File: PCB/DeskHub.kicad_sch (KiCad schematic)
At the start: 67 parts, among them J1 USB_A, J2 5V Barrel, U1 TUSB4041I, U2 3.3V Reg, U3 1.1V Reg, Y1 24MHz

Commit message: Completed schematic!
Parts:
- added R15, R20, R21, R22, R23, R24, R25, R26: 4.7K, symbol Device:R_Small
- added R27: 10K, symbol Device:R_Small
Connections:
- net BOARD_3.3V: now also R23.2, R24.2, R25.2, R26.2, R27.1
- net Earth: now also U1.65 (VSS), R15.2, R20.2, R21.2, R22.2
- net Port 1 Power Switch/PWRON_EN: now also R26.1
- net Port 2 Power Switch/PWRON_EN: now also R25.1
- net Port 3 Power Switch/PWRON_EN: now also R24.1
- net Port 4 Power Switch/PWRON_EN: now also R23.1
- net at U1.10 (GANGED/SMBA2/HS_UP): now also R21.1
- net at U1.13 (AUTOENz/HS_SUSPEND): now also R15.1
- net at U1.17 (TEST): now also R20.1
- net at U1.8 (FULLPWRMGMTz/SMBA1): now also R22.1
- net at U1.9 (PWRCTL_POL): now also R27.2
- no-connect marks 1 -> 4

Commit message: adjust schematic to match real components, assign footprints
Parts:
- removed Y1: 24MHz, symbol Device:Crystal
- added Y1: ECS-240-20-30B-TR, my_global:XTAL_ECS-240-20-30B-TR, symbol ECS-240-20-30B-TR:ECS-240-20-30B-TR
- C1, C16, C17, C43: footprint (none) -> Capacitor_SMD:C_0402_1005Metric
- C10, C11, C12, C18, C19, C2, C20, C21, C22, C23, C24, C25, C26, C28, C29, C3, C30, C31, C32, C33, C34, C35, C36, C37, C38, C39, C4, C40, C41, C5, C6, C7, C8, C9: footprint (none) -> Capacitor_SMD:C_0201_0603Metric
- C13, C14: value 18pF TODO -> 18pF; footprint (none) -> Capacitor_SMD:C_0402_1005Metric
- C15, C27, C42, C45, C46, C47: footprint (none) -> Capacitor_SMD:C_1206_3216Metric
- C44: footprint (none) -> Capacitor_SMD:C_0805_2012Metric
- D1, D2: footprint (none) -> LED_SMD:LED_0603_1608Metric
- FB5, FB6: footprint (none) -> my_global:BEADC1608X95N
- J1: footprint (none) -> my_global:61400416021; symbol Connector:USB_A -> 61400416021:61400416021
- J2: footprint (none) -> my_global:694108301002; symbol Connector:Barrel_Jack -> 694108301002:694108301002
- R1, R10, R15, R2, R20, R21, R22, R23, R24, R25, R26, R27, R3, R4, R5, R6, R7, R8, R9: footprint (none) -> Resistor_SMD:R_0402_1005Metric
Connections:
- net Earth: now also J2.3
- net GNDPWR: now also J1.S1, J1.S2; no longer J1.5 (Shield)
- net XI: now also Y1.3 (OUT/IN)
- net XO: now also Y1.1 (IN/OUT)
- no-connect marks 4 -> 6
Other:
- note added: "Crystal"
- note removed: "Crystal TODO calculate capacitor values"
- moved on the sheet: C13, C15

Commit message: final save of the night
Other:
- note added: "Design Notes - differential impedance of 90 Ohm - each differential pair should be 5*trace width apart - route all pairs on same layer, next to ground plane - avoid 90 degree bends, keep left and right bends equal - differential pairs should not exceed 50 mils relative distance"
- note removed: "Design Notes - differential impedance of 90Ohm - each differential pair should be 5*trace width apart - route all pairs on same layer, next to ground plane - avoid 90 degree bends, keep left and right bends equal - differential pairs should not exceed 50 mils relative distance"
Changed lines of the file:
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@@
 		)
 	)
-	(text "Design Notes\n\n- differential impedance of 90Ohm\n- each differential pair should be 5*trace width apart \n- route all pairs on same layer, next to ground plane\n- avoid 90 degree bends, keep left and right bends equal\n- differential pairs should not exceed 50 mils relative distance\n"
+	(text "Design Notes\n\n- differential impedance of 90 Ohm\n- each differential pair should be 5*trace width apart \n- route all pairs on same layer, next to ground plane\n- avoid 90 degree bends, keep left and right bends equal\n- differential pairs should not exceed 50 mils relative distance\n"
 		(exclude_from_sim no)
 		(at 124.46 -11.43 0)

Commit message: saved
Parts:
- C22: footprint Capacitor_SMD:C_0201_0603Metric -> Capacitor_SMD:C_1206_3216Metric
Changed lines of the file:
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@@
 		(polyline
 			(pts
-				(xy 171.45 138.43) (xy 171.45 143.51) (xy 172.72 143.51) (xy 172.72 138.43)
+				(xy 172.72 125.73) (xy 172.72 130.81) (xy 173.99 130.81) (xy 173.99 125.73)
 			)
 			(stroke
@@
 		(polyline
 			(pts
-				(xy 171.45 151.13) (xy 171.45 156.21) (xy 172.72 156.21) (xy 172.72 151.13)
+				(xy 171.45 163.83) (xy 171.45 168.91) (xy 172.72 168.91) (xy 172.72 163.83)
 			)
 			(stroke
@@
 		(polyline
 			(pts
-				(xy 172.72 125.73) (xy 172.72 130.81) (xy 173.99 130.81) (xy 173.99 125.73)
+				(xy 171.45 138.43) (xy 171.45 143.51) (xy 172.72 143.51) (xy 172.72 138.43)
 			)
 			(stroke
@@
 		(polyline
 			(pts
-				(xy 171.45 163.83) (xy 171.45 168.91) (xy 172.72 168.91) (xy 172.72 163.83)
+				(xy 171.45 151.13) (xy 171.45 156.21) (xy 172.72 156.21) (xy 172.72 151.13)
 			)
 			(stroke
@@
 			)
 		)
-		(property "Footprint" "Capacitor_SMD:C_0201_0603Metric"
+		(property "Footprint" "Capacitor_SMD:C_1206_3216Metric"
 			(at 29.21 26.67 0)
 			(effects

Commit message: pcb v2.01 reddit review post
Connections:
- net XI: no longer names the net of C14.1, R2.2, U1.30 (XI), Y1.3 (OUT/IN)
- net XO: no longer names the net of C13.1, R2.1, U1.29 (XO), Y1.1 (IN/OUT)
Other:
- title: TUSB4041PAP -> Desk Hub 
- moved on the sheet: C1, C10, C11, C12, C13, C14, C15, C16, C17, C18, C19, C2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

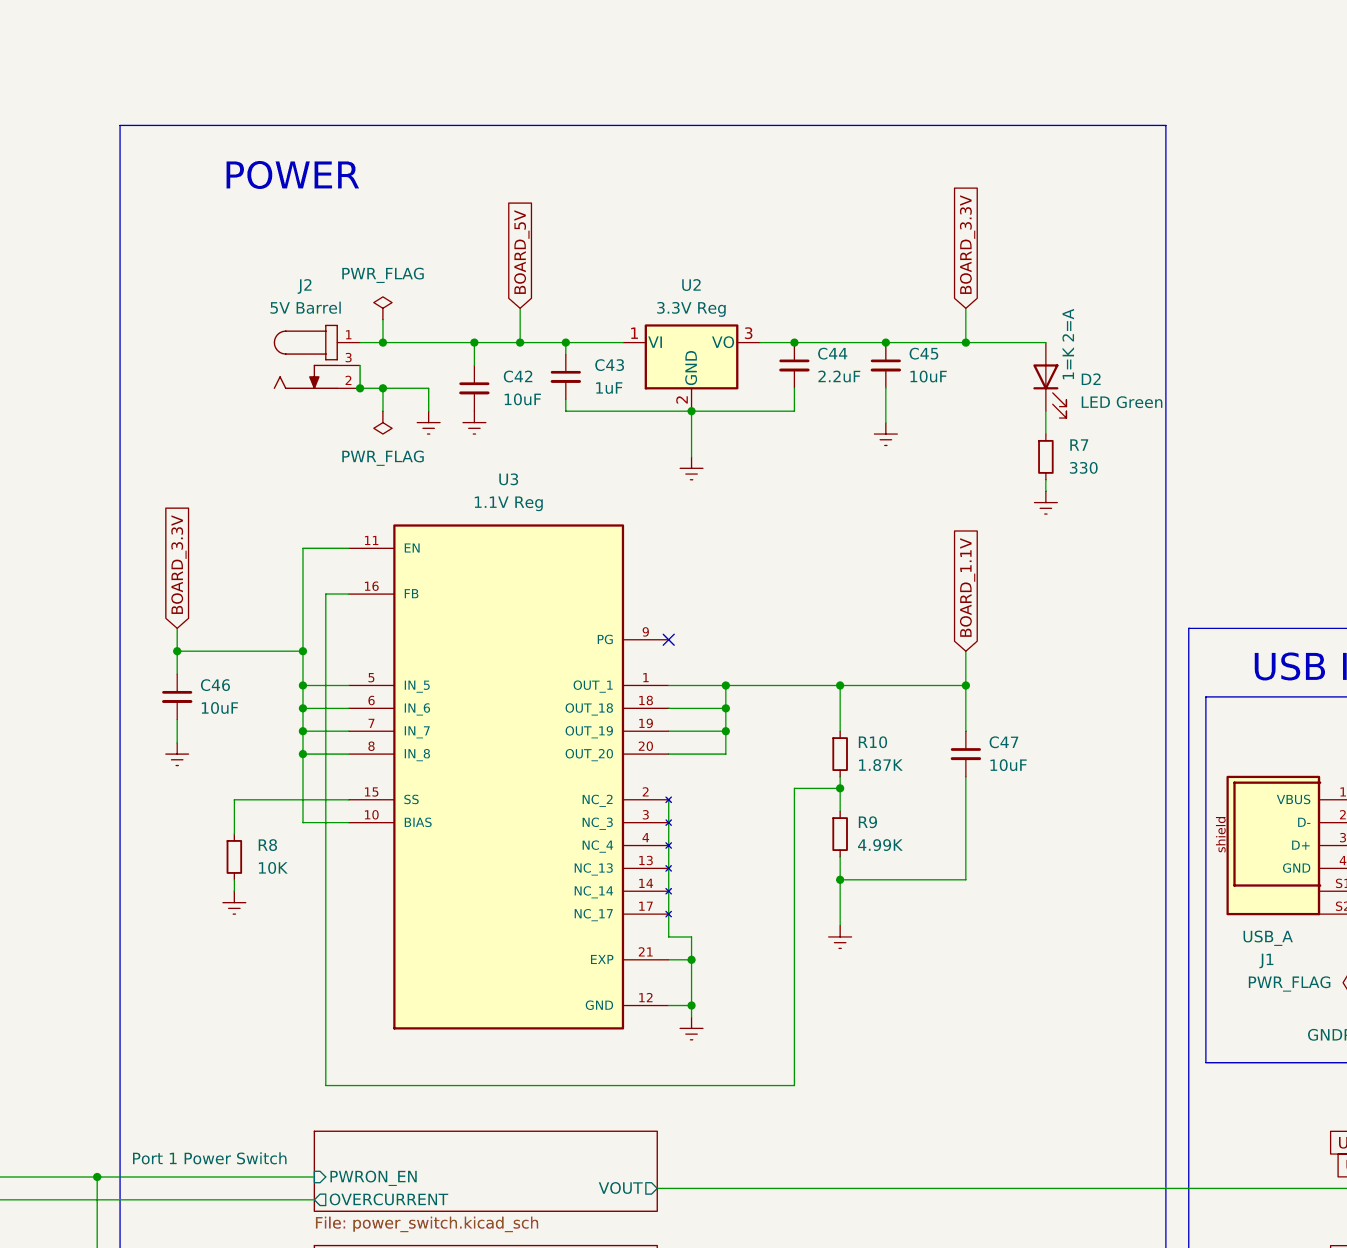
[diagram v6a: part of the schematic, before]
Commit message: switching vreg
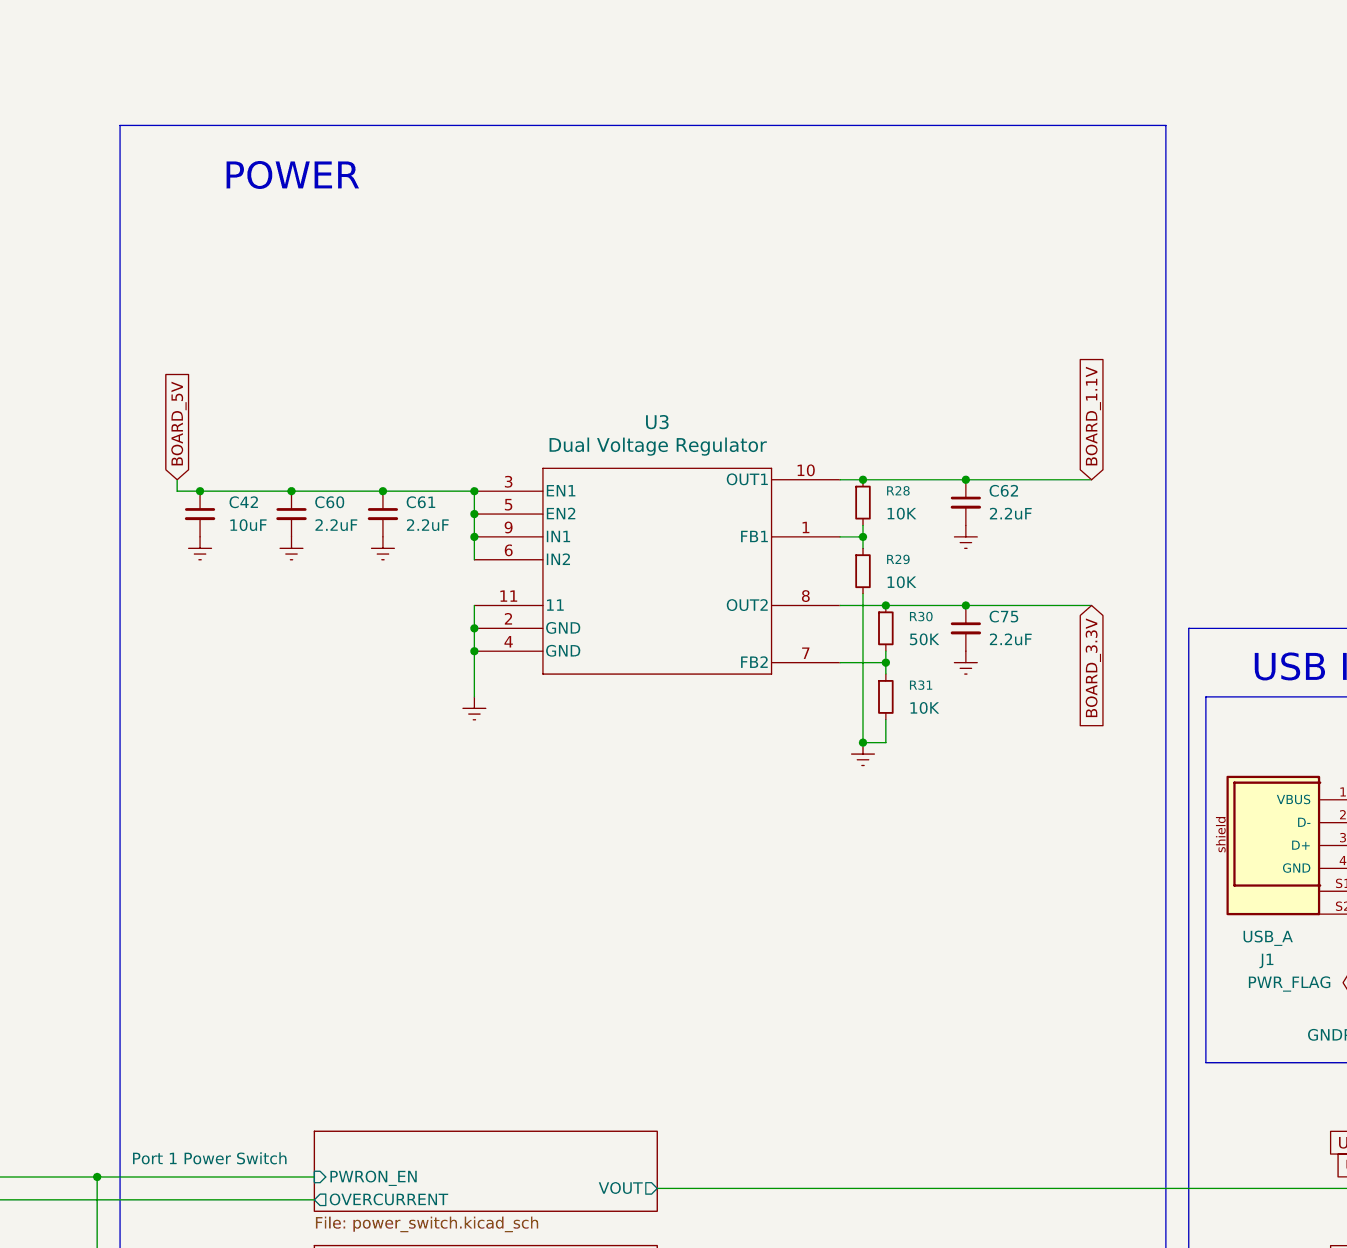
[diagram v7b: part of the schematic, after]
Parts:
- removed C43: 1uF, Capacitor_SMD:C_0402_1005Metric, symbol Device:C_Small
- removed C44: 2.2uF, Capacitor_SMD:C_0805_2012Metric, symbol Device:C_Small
- removed C45, C46, C47: 10uF, Capacitor_SMD:C_1206_3216Metric, symbol Device:C_Small
- removed D2: LED Green, LED_SMD:LED_0603_1608Metric, symbol Device:LED
- removed J2: 5V Barrel, my_global:694108301002, symbol 694108301002:694108301002
- removed R10: 1.87K, Resistor_SMD:R_0402_1005Metric, symbol Device:R_Small
- removed R7: 330, Resistor_SMD:R_0402_1005Metric, symbol Device:R_Small
- removed R8: 10K, Resistor_SMD:R_0402_1005Metric, symbol Device:R_Small
- removed R9: 4.99K, Resistor_SMD:R_0402_1005Metric, symbol Device:R_Small
- removed U2: 3.3V Reg, Package_TO_SOT_SMD:TO-252-3_TabPin2, symbol Regulator_Linear:LD39150DT33
- removed U3: 1.1V Reg, my_global:QFN65P500X500X100-21N, symbol my_global:TPS74801RGWR
- added C60, C61, C62, C75: 2.2uF, Capacitor_SMD:C_0805_2012Metric, symbol Device:C_Small
- added R28, R29, R31: 10K, symbol Device:R_Small
- added R30: 50K, symbol Device:R_Small
- added U3: Dual Voltage Regulator, my_global:SON_1PDSQR_TEX, symbol my_global:TLV75201PDSQR
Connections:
- net BOARD_1.1V: now also C62.1, R28.1, U3.10 (OUT1)
- net BOARD_3.3V: now also C75.1, R30.1, U3.8 (OUT2)
- net BOARD_5V: now also C60.1, C61.1, U3.3 (EN1), U3.5 (EN2), U3.6 (IN2), U3.9 (IN1)
- net Earth: now also C60.2, C61.2, C62.2, C75.2, R29.2, R31.2, U3.11, U3.2 (GND), U3.4 (GND)
- new net: R28.2, R29.1, U3.1 (FB1)
- new net: R30.2, R31.1, U3.7 (FB2)
- no-connect marks 6 -> 5
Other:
- moved on the sheet: C42

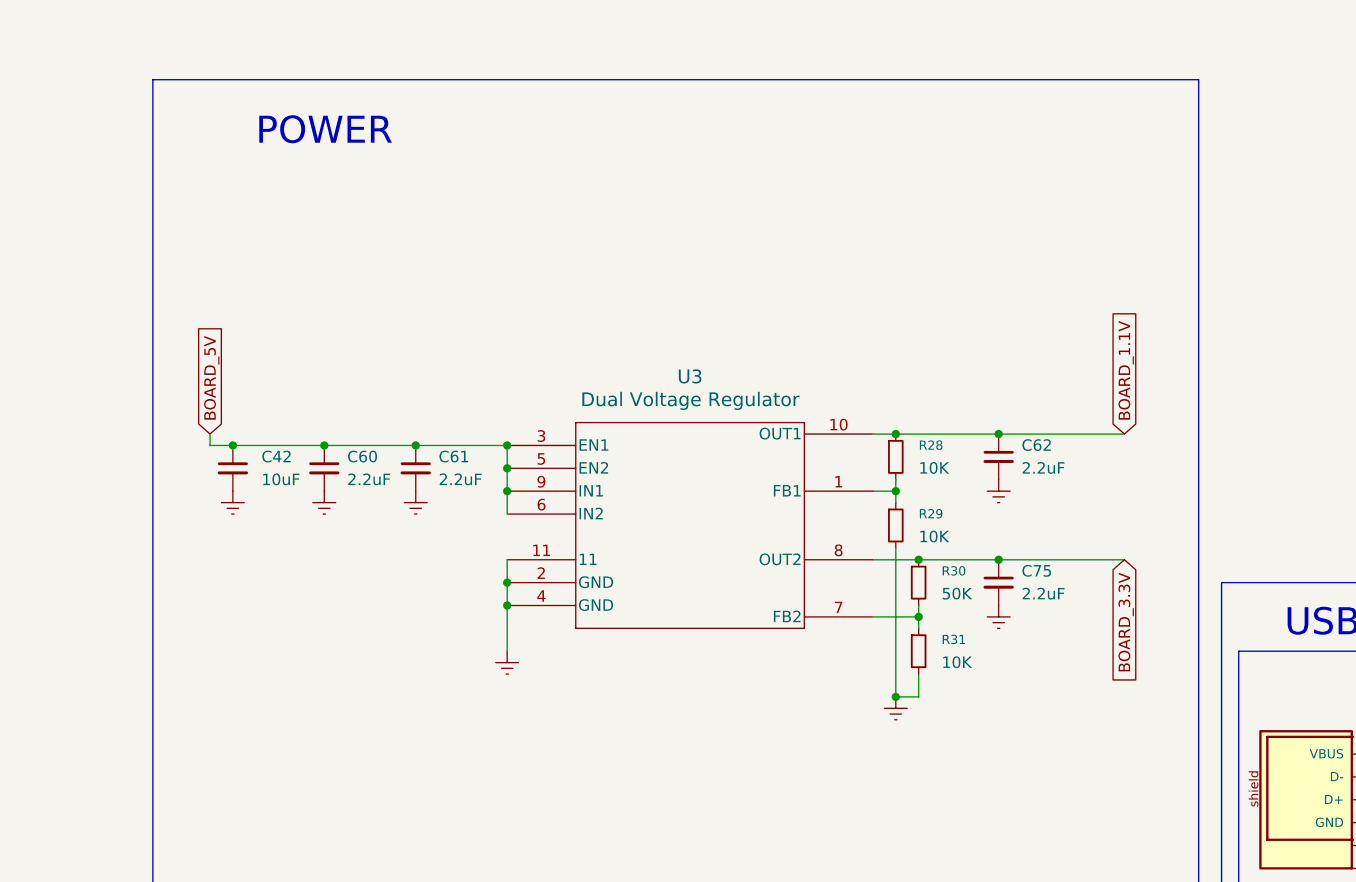
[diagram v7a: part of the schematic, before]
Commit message: add back barrel jack
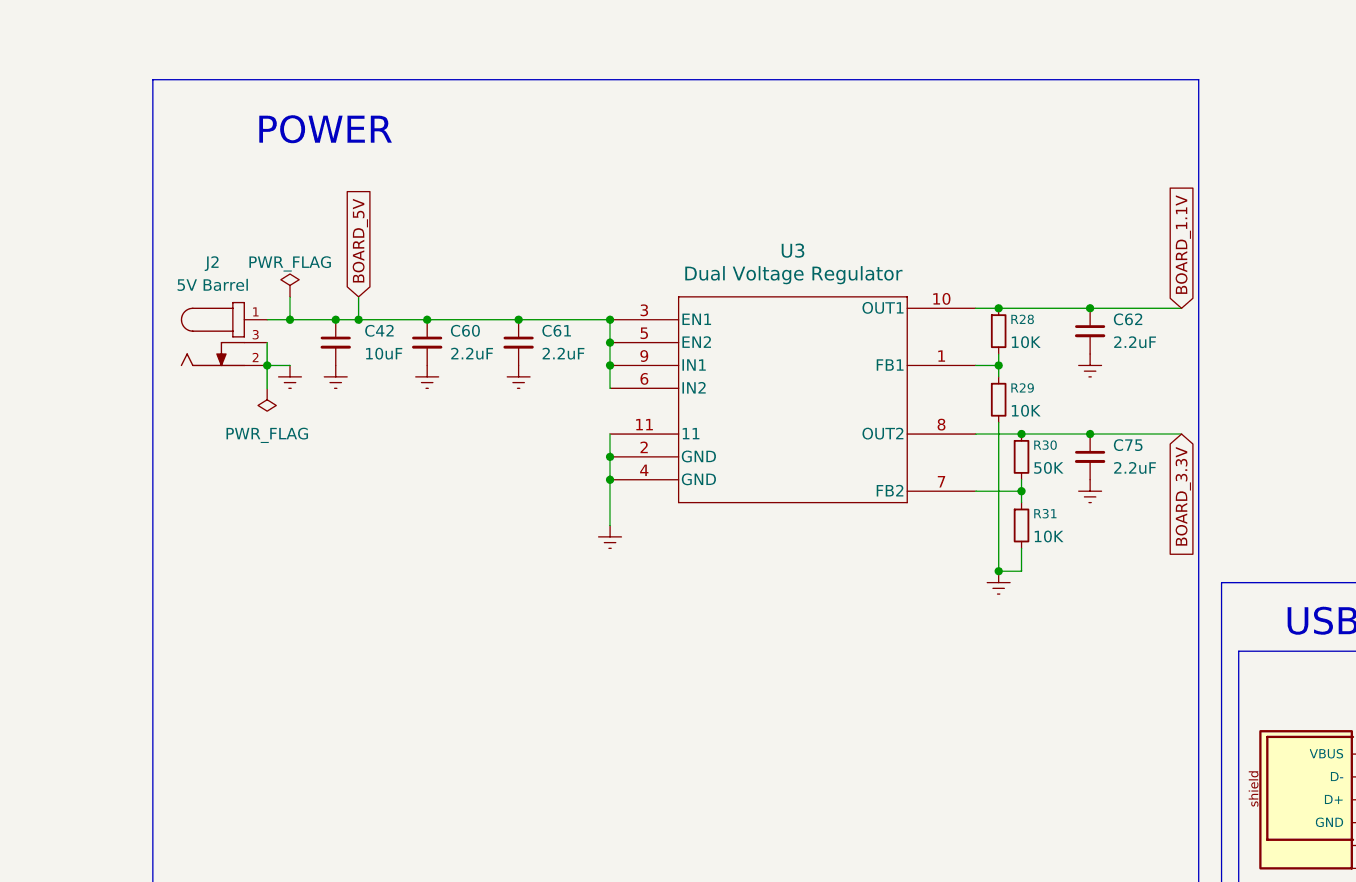
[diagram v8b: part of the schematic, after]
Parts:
- added J2: 5V Barrel, my_global:694108301002, symbol 694108301002:694108301002
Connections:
- net BOARD_5V: now also J2.1
- net Earth: now also J2.2, J2.3
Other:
- moved on the sheet: C42, C60, C61, C62, C75, R28, R29, R30, R31, U3
